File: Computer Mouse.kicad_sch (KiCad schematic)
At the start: 37 parts, among them J1 USB_C_Receptacle_USB2.0, J2 Conn_01x02, Q1 MMDT3906, Q2 MMDT3906, Q3 MMDT3906, Q4 MMDT3906, SW1 SW_SPDT, SW2 SW_SPDT, SW3 SW_SPDT, SW4 SW_SPDT, SW5 SW_SPST, SW6 RotaryEncoder, SW7 RotaryEncoder, U2 MCP73831-2-OT, U3 STM32F103RCT6

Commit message: BT module
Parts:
- added U6: RN4871, RF_Module:ST_SPBTLE, symbol RF_Bluetooth:RN4871
- J1: footprint (none) -> Connector_USB:USB_C_Receptacle_GCT_USB4085
- J2: footprint (none) -> Connector_JST:JST_EH_B2B-EH-A_1x02_P2.50mm_Vertical
- renumbered C3 to C4, C3 to C5, C3 to C6, C3 to C7, R3 to R10, R3 to R4, R4 to R5, R5 to R6, R3 to R7, R3 to R8, R3 to R9, U3 to U2, U2 to U4
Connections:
- net +3V3: now also U6.14 (VBAT)
- net GND: now also U6.13 (GND), U6.2 (GND)
- net BT_UART_CTS: now reaches U2.2 (PC13)
- net BT_UART_CTS: now also U6.11 (P0_0)
- net BT_P2_0: now reaches U2.29 (PB10)
- net BT_P2_0: now also U6.16 (P2_0)
- net BT_UART_RST: now reaches U2.3 (PC14)
- net BT_UART_RST: now also U6.9 (P3_6)
- net BT_P1_2: now reaches U2.30 (PB11)
- net BT_P1_2: now also U6.3 (P1_2)
- net BT_P1_3: now reaches U2.33 (PB12)
- net BT_P1_3: now also U6.4 (P1_3)
- net BT_P1_7: now reaches U2.34 (PB13)
- net BT_P1_7: now also U6.5 (P1_7)
- net BT_P1_6: now reaches U2.35 (PB14)
- net BT_P1_6: now also U6.6 (P1_6)
- net BT_P0_2: now reaches U2.36 (PB15)
- net BT_P0_2: now also U6.12 (P0_2)
- net BT_UART_TX_IND: now reaches U2.4 (PC15)
- net BT_UART_TX_IND: now also U6.15 (P2_7)
- net BT_RX: now reaches U2.51 (PC10)
- net BT_RX: now also U6.7 (UART_RX)
- net BT_TX: now reaches U2.52 (PC11)
- net BT_TX: now also U6.8 (UART_TX)
- net BT_RST: now reaches U2.53 (PC12)
- net BT_RST: now also U6.10 (RST)
- no-connect marks 34 -> 23
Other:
- note added: "BT module"
- note added: "For ERC"
- moved on the sheet: C1, C2, C3, C4, C5, C6, C7, D1, D2, J1, J2, L1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

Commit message: ERC fix
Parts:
- removed Q1, Q2, Q3, Q4: MMDT3906, Package_TO_SOT_SMD:SOT-363_SC-70-6, symbol Transistor_BJT:MMDT3906
- added Q1, Q2, Q3, Q4: 2N3905, Package_TO_SOT_THT:TO-92_Inline, symbol Transistor_BJT:2N3905
- renumbered C3 to C2, C2 to C3, C7 to C5, C5 to C6, C6 to C7, R5 to R1, R7 to R10, R6 to R2, R4 to R3, R1 to R4, R2 to R5, R10 to R6, R3 to R7, R9 to R8, R8 to R9, SW5 to SW1, SW3 to SW2, SW1 to SW3, SW2 to SW4, SW4 to SW5, U4 to U2, U6 to U3, U3 to U4, U2 to U5
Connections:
- net +3V3: now also C4.1, U4.7 (VDDIO), Q1.1 (E), Q2.1 (E), Q3.1 (E), Q4.1 (E)
- net at U5.55 (PB3): now also Q3.2 (B)
- net at R8.1: now also Q3.3 (C)
- net at U5.16 (PA2): now also Q4.2 (B)
- net at R10.1: now also Q4.3 (C)
- net at R7.1: now also Q1.3 (C)
- net at U4.8 (XYLED): now also Q1.2 (B)
- net at R9.1: now also Q2.3 (C)
- net at U5.50 (PA15): now also Q2.2 (B)
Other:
- moved on the sheet: D1, R7

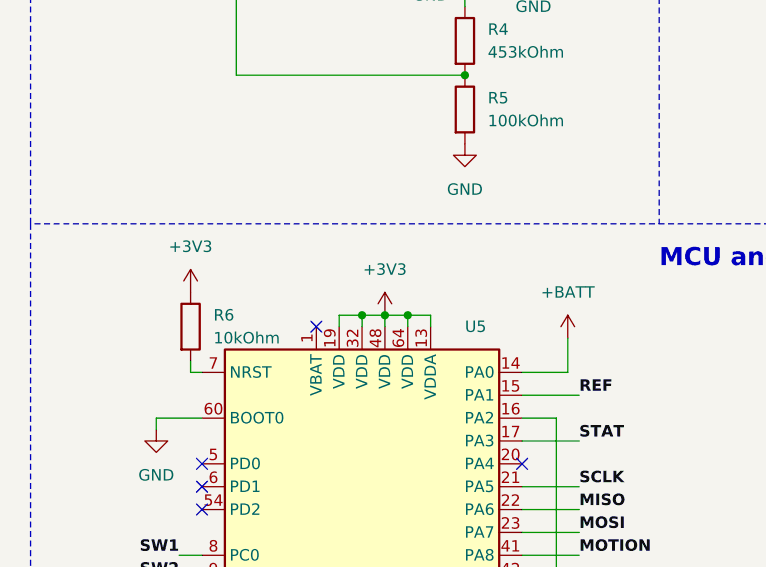
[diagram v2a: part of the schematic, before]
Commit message: New footprints
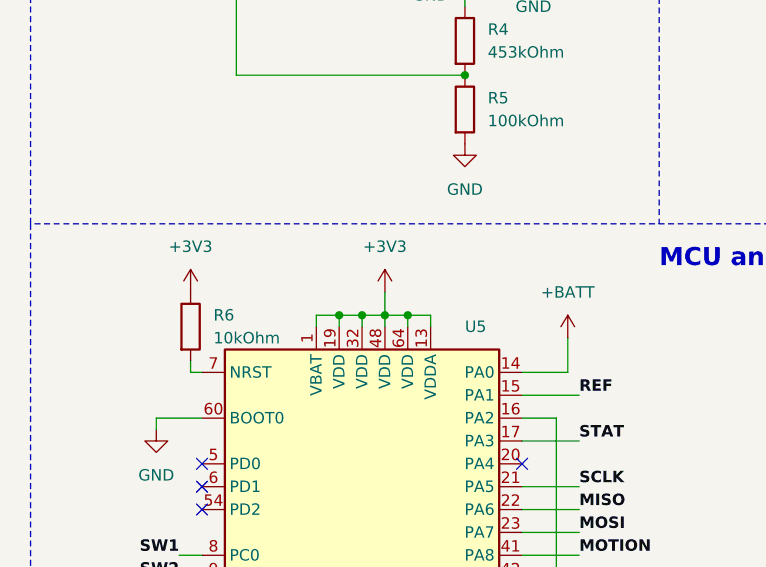
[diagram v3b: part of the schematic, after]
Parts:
- C1, C2, C3, C4, C5, C6: footprint (none) -> Capacitor_THT:CP_Radial_D5.0mm_P2.00mm
- C7: footprint (none) -> Capacitor_THT:C_Disc_D6.0mm_W2.5mm_P5.00mm
- D1: footprint (none) -> LED_THT:LED_D5.0mm_Horizontal_O1.27mm_Z3.0mm_Clear
- D2: footprint (none) -> LED_THT:LED_D5.0mm-4_RGB
- J1: footprint Connector_USB:USB_C_Receptacle_GCT_USB4085 -> Connector_USB:USB_C_Receptacle_GCT_USB4105-xx-A_16P_TopMnt_Horizontal
- L1: footprint (none) -> Inductor_SMD:L_0603_1608Metric_Pad1.05x0.95mm_HandSolder
- R1, R10, R2, R3, R4, R5, R6, R7, R8, R9: footprint (none) -> Resistor_THT:R_Axial_DIN0207_L6.3mm_D2.5mm_P7.62mm_Horizontal
- SW1: footprint (none) -> Button_Switch_THT:SW_DIP_SPSTx01_Slide_6.7x4.1mm_W7.62mm_P2.54mm_LowProfile
- SW2, SW3, SW4, SW5: footprint (none) -> Omron_switch_mouse:Mouse_Switch
- SW6, SW7: footprint (none) -> TTC_Rotary_Encoder:TTC_rotary_encoder
- U1: footprint (none) -> TPS61023:TPS61023_DC_DC
- U4: footprint (none) -> PMW3310:PMW3110DH-AWQT
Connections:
- net +3V3: now also U5.1 (VBAT)
- no-connect marks 23 -> 22

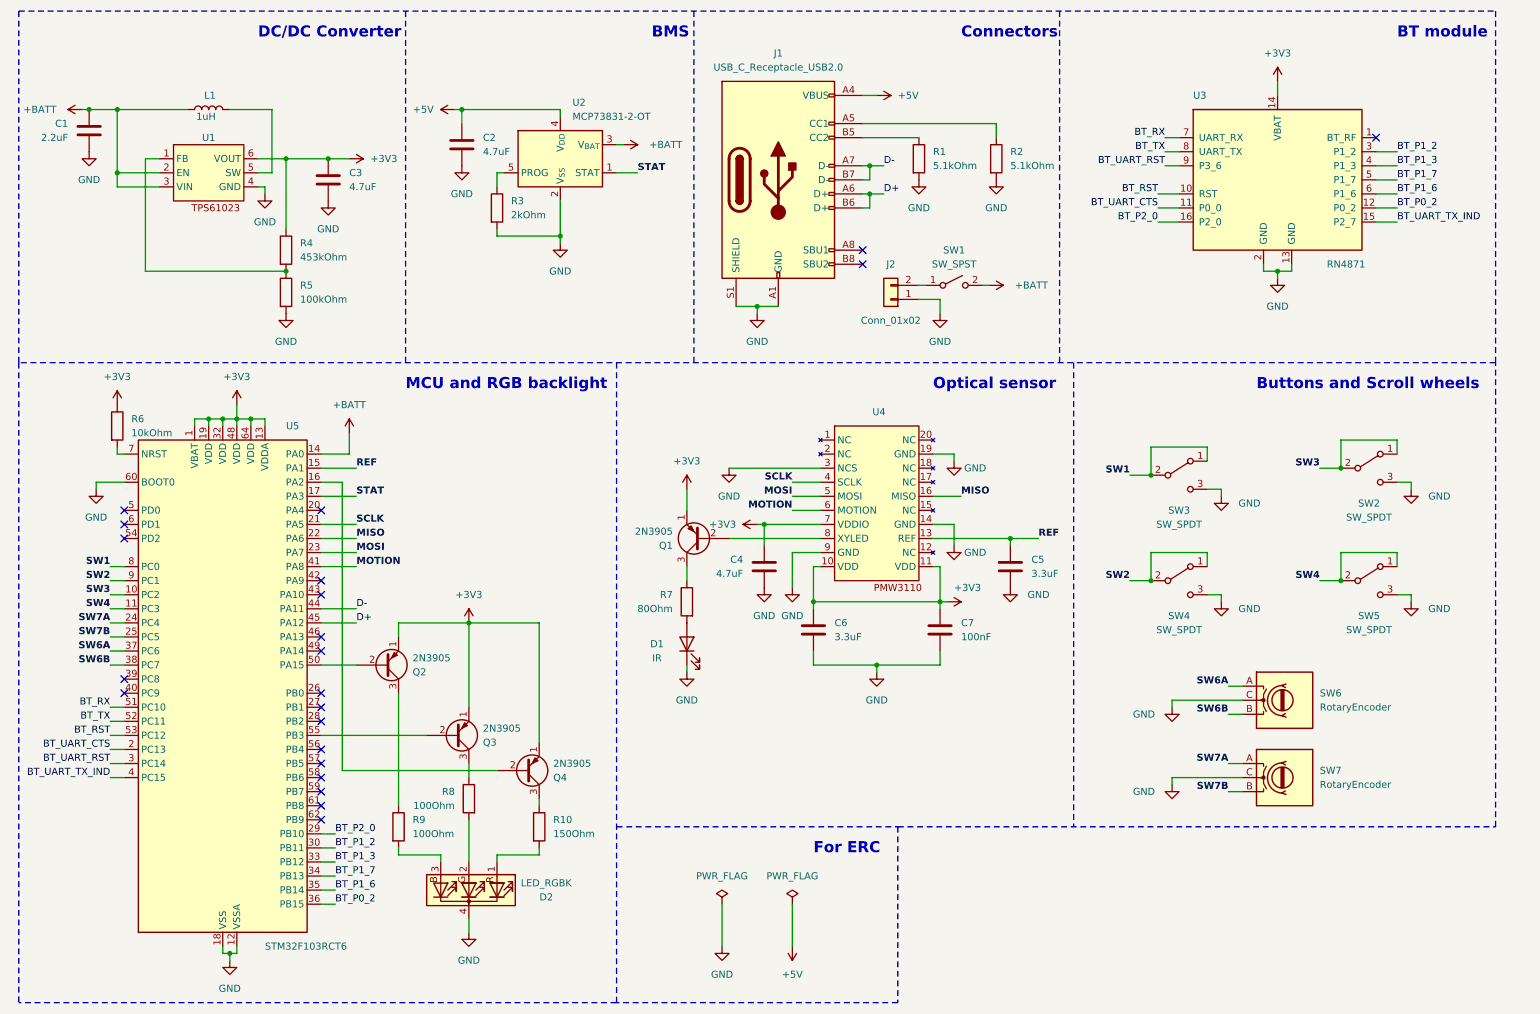
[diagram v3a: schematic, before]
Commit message: New layout, pull-up resistors, filters, decoupling capacitors
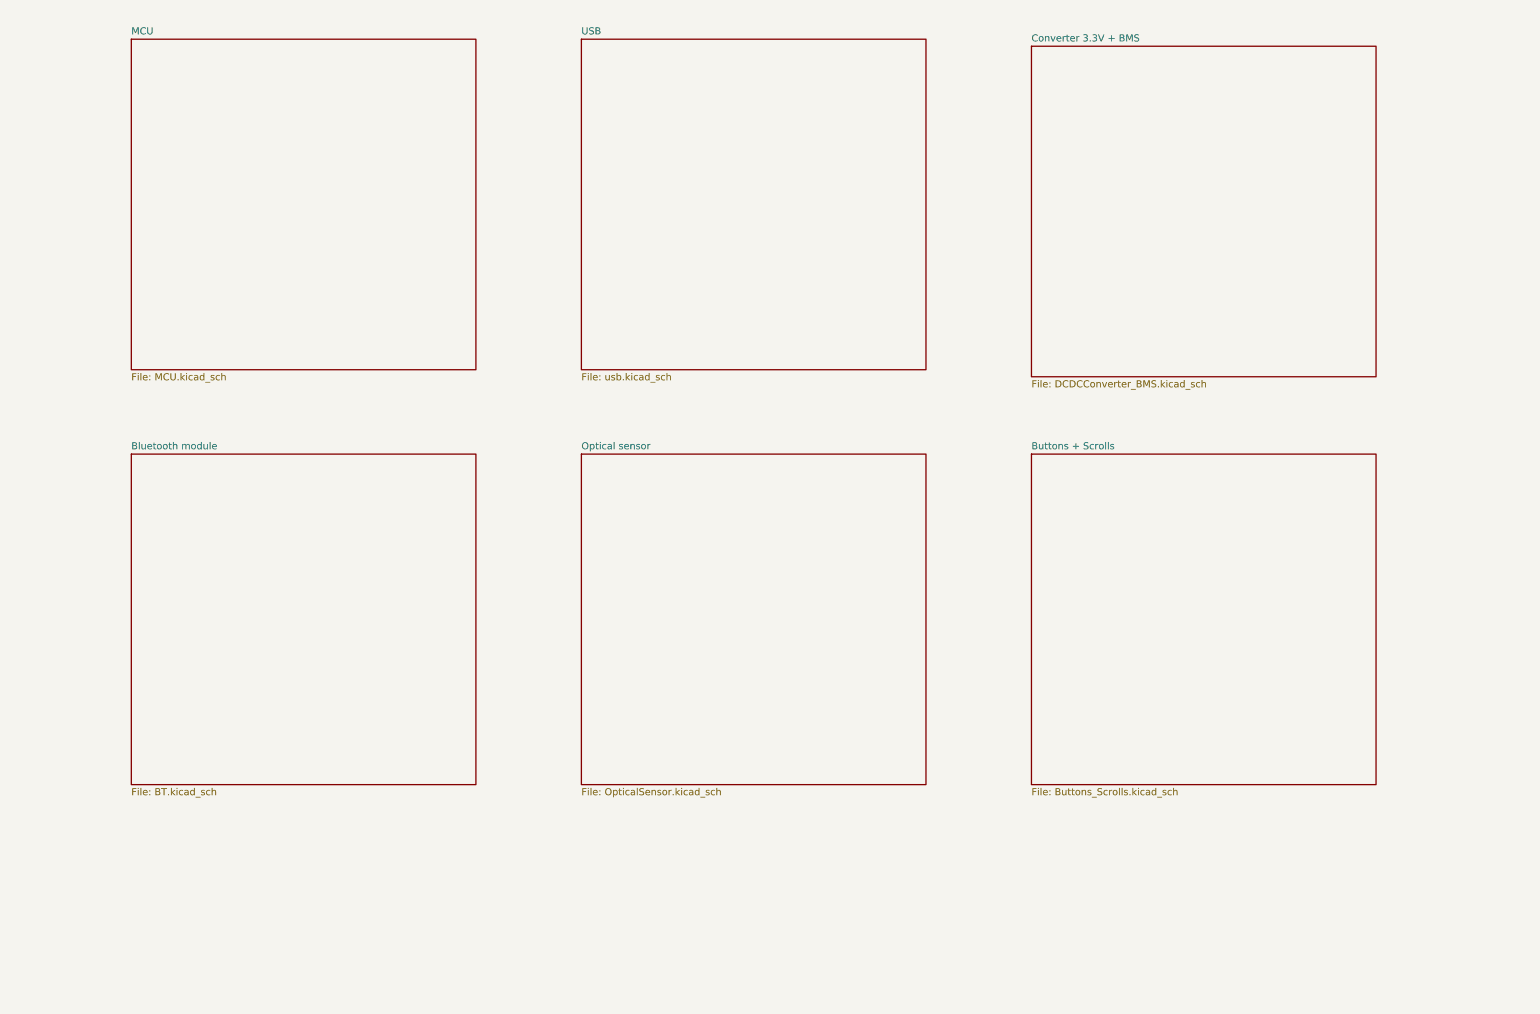
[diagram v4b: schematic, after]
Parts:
- removed C1: 2.2uF, Capacitor_THT:CP_Radial_D5.0mm_P2.00mm, symbol Device:C
- removed C2, C3, C4: 4.7uF, Capacitor_THT:CP_Radial_D5.0mm_P2.00mm, symbol Device:C
- removed C5, C6: 3.3uF, Capacitor_THT:CP_Radial_D5.0mm_P2.00mm, symbol Device:C
- removed C7: 100nF, Capacitor_THT:C_Disc_D6.0mm_W2.5mm_P5.00mm, symbol Device:C
- removed D1: IR, LED_THT:LED_D5.0mm_Horizontal_O1.27mm_Z3.0mm_Clear, symbol Device:LED
- removed D2: LED_RGBK, LED_THT:LED_D5.0mm-4_RGB, symbol Device:LED_RGBK
- removed J1: USB_C_Receptacle_USB2.0, Connector_USB:USB_C_Receptacle_GCT_USB4105-xx-A_16P_TopMnt_Horizontal, symbol Connector:USB_C_Receptacle_USB2.0
- removed J2: Conn_01x02, Connector_JST:JST_EH_B2B-EH-A_1x02_P2.50mm_Vertical, symbol Connector_Generic:Conn_01x02
- removed L1: 1uH, Inductor_SMD:L_0603_1608Metric_Pad1.05x0.95mm_HandSolder, symbol Device:L
- removed Q1, Q2, Q3, Q4: 2N3905, Package_TO_SOT_THT:TO-92_Inline, symbol Transistor_BJT:2N3905
- removed R1, R2: 5.1kOhm, Resistor_THT:R_Axial_DIN0207_L6.3mm_D2.5mm_P7.62mm_Horizontal, symbol Device:R
- removed R10: 150Ohm, Resistor_THT:R_Axial_DIN0207_L6.3mm_D2.5mm_P7.62mm_Horizontal, symbol Device:R
- removed R3: 2kOhm, Resistor_THT:R_Axial_DIN0207_L6.3mm_D2.5mm_P7.62mm_Horizontal, symbol Device:R
- removed R4: 453kOhm, Resistor_THT:R_Axial_DIN0207_L6.3mm_D2.5mm_P7.62mm_Horizontal, symbol Device:R
- removed R5: 100kOhm, Resistor_THT:R_Axial_DIN0207_L6.3mm_D2.5mm_P7.62mm_Horizontal, symbol Device:R
- removed R6: 10kOhm, Resistor_THT:R_Axial_DIN0207_L6.3mm_D2.5mm_P7.62mm_Horizontal, symbol Device:R
- removed R7: 80Ohm, Resistor_THT:R_Axial_DIN0207_L6.3mm_D2.5mm_P7.62mm_Horizontal, symbol Device:R
- removed R8, R9: 100Ohm, Resistor_THT:R_Axial_DIN0207_L6.3mm_D2.5mm_P7.62mm_Horizontal, symbol Device:R
- removed SW1: SW_SPST, Button_Switch_THT:SW_DIP_SPSTx01_Slide_6.7x4.1mm_W7.62mm_P2.54mm_LowProfile, symbol Switch:SW_SPST
- removed SW2, SW3, SW4, SW5: SW_SPDT, Omron_switch_mouse:Mouse_Switch, symbol Switch:SW_SPDT
- removed SW6, SW7: RotaryEncoder, TTC_Rotary_Encoder:TTC_rotary_encoder, symbol Device:RotaryEncoder
- removed U1: ~, TPS61023:TPS61023_DC_DC, symbol TPS61023DCDCConverter:TPS61023
- removed U2: MCP73831-2-OT, Package_TO_SOT_SMD:SOT-23-5, symbol Battery_Management:MCP73831-2-OT
- removed U3: RN4871, RF_Module:ST_SPBTLE, symbol RF_Bluetooth:RN4871
- removed U4: ~, PMW3310:PMW3110DH-AWQT, symbol PMW3110:PMW3110
- removed U5: STM32F103RCT6, Package_QFP:LQFP-64_10x10mm_P0.5mm, symbol MCU_ST_STM32F1:STM32F103RCTx
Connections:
- no-connect marks 22 -> 0
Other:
- added sheet Bluetooth module (BT.kicad_sch)
- added sheet Buttons + Scrolls (Buttons_Scrolls.kicad_sch)
- added sheet Converter 3.3V + BMS (DCDCConverter_BMS.kicad_sch)
- added sheet MCU (MCU.kicad_sch)
- added sheet Optical sensor (OpticalSensor.kicad_sch)
- added sheet USB (usb.kicad_sch)
- note removed: "BMS"
- note removed: "BT module"
- note removed: "Buttons and Scroll wheels"
- note removed: "Connectors"
- note removed: "DC/DC Converter"
- note removed: "For ERC"
- note removed: "MCU and RGB backlight"
- note removed: "Optical sensor"

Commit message: GND fields
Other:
- company: (none) -> Piotr Zborowski, Łukasz Kus
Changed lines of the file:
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@@
   (title_block
     (title "Gaming Mouse")
+    (date "2024-01-02")
+    (rev "v1.1")
+    (company "Piotr Zborowski, Łukasz Kus")
   )
   (sheet (at 116.84 20.32) (size 62.23 59.69) (fields_autoplaced)
